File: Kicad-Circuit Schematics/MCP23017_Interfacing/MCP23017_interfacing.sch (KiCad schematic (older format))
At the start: 12 parts, among them SW1 SW_PUSH

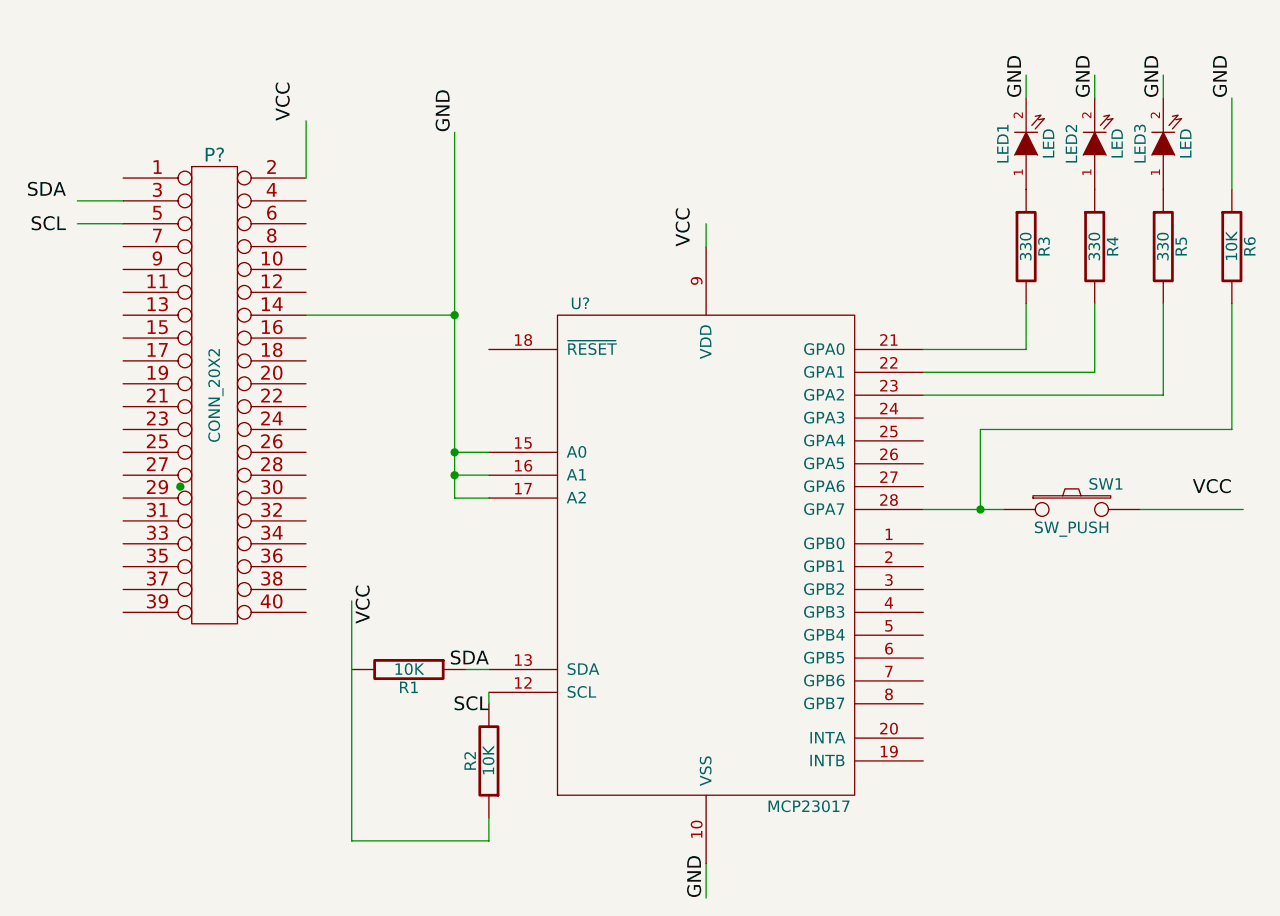
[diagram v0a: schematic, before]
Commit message: Schematics
Consists of schematics of 3 different circuits (led & push button, lcd
circuit and motor circuits)
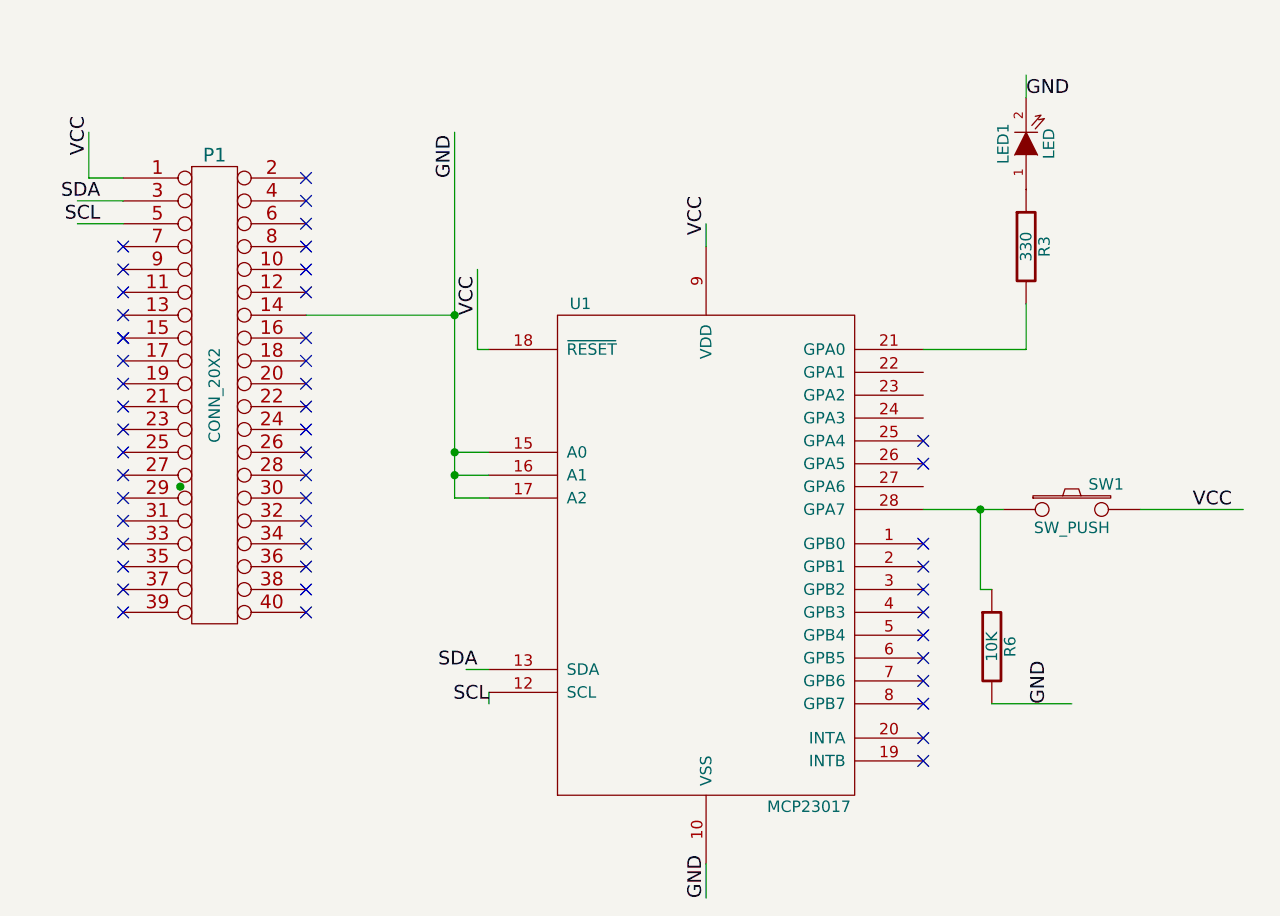
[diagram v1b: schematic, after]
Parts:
- removed LED2, LED3: LED, symbol LED
- removed R1, R2: 10K, symbol R
- removed R4, R5: 330, symbol R
- gave numbers to parts that had none: 2
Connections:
- wire segments 30 -> 23
- no-connect marks 0 -> 49
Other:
- moved on the sheet: R6
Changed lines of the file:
@@
-EESchema Schematic File Version 2  date 16-Jun-15 2:01:25 AM
+EESchema Schematic File Version 2  date 26/06/2015 16:15:03
 LIBS:power
 LIBS:device
@@
 LIBS:contrib
 LIBS:valves
-LIBS:analogSpice
-LIBS:analogXSpice
-LIBS:convergenceAidSpice
-LIBS:converterSpice
-LIBS:digitalSpice
-LIBS:digitalXSpice
-LIBS:linearSpice
-LIBS:measurementSpice
-LIBS:portSpice
-LIBS:sourcesSpice
 LIBS:MCP23017
-EELAYER 43  0
+LIBS:MCP23017_interfacing-cache
+EELAYER 25  0
 EELAYER END
 $Descr A4 11700 8267
@@
 Sheet 1 1
 Title ""
-Date "15 jun 2015"
+Date "26 jun 2015"
 Rev ""
 Comp ""
@@
 Comment4 ""
 $EndDescr
-Text Label 5250 4250 2    60   ~ 0
-SCL
-Text Label 5250 4050 2    60   ~ 0
-SDA
-Text Label 4750 3850 1    60   ~ 0
-VCC
-Wire Wire Line
-	4650 4800 5250 4800
-Wire Wire Line
-	4650 3750 4650 4800
+Text Label 6200 2150 1    60   ~ 0
+VCC
+Wire Wire Line
+	5200 2300 5200 2650
+Wire Wire Line
+	5200 2650 5250 2650
+Wire Wire Line
+	5100 1700 5100 3300
 Connection ~ 5100 3200
 Wire Wire Line
-	5250 3300 5100 3300
-Wire Wire Line
-	4450 1900 4450 1650
+	5100 3300 5250 3300
 Connection ~ 7400 3350
 Wire Wire Line
-	7400 3350 7400 3000
-Wire Wire Line
-	7400 3000 8500 3000
-Wire Wire Line
-	8500 3000 8500 2450
-Wire Wire Line
 	8100 3350 8550 3350
 Wire Wire Line
 	6200 2200 6200 2100
 Wire Wire Line
-	7900 1550 7900 1450
-Wire Wire Line
-	8200 2450 8200 2850
-Wire Wire Line
-	8200 2850 7150 2850
-Wire Wire Line
 	7600 2450 7600 2650
 Wire Wire Line
@@
 Wire Wire Line
 	6200 4900 6200 5050
-Wire Wire Line
-	5250 4800 5250 4700
 Wire Wire Line
 	5100 2500 4450 2500
@@
 	3650 2100 3450 2100
 Wire Wire Line
-	7150 2750 7900 2750
-Wire Wire Line
-	7900 2750 7900 2450
-Wire Wire Line
 	7600 1550 7600 1450
 Wire Wire Line
-	8200 1550 8200 1450
-Wire Wire Line
 	7500 3350 7150 3350
-Wire Wire Line
-	8500 1550 8500 1950
 Wire Wire Line
 	5100 3100 5250 3100
@@
 	5100 3200 5250 3200
 Connection ~ 5100 3100
-Wire Wire Line
-	5100 3300 5100 1700
 Connection ~ 5100 2500
-$Comp
-L MCP23017 U?
+Wire Wire Line
+	7400 3350 7400 3700
+Wire Wire Line
+	7400 3700 7450 3700
+Wire Wire Line
+	7450 4200 7800 4200
+Wire Wire Line
+	3650 1900 3500 1900
+Wire Wire Line
+	3500 1900 3500 1700
+Text Label 7600 1550 0    60   ~ 0
+GND
+NoConn ~ 7150 3050
+NoConn ~ 7150 3150
+NoConn ~ 4450 1900
+NoConn ~ 4450 2100
+NoConn ~ 4450 2200
+NoConn ~ 4450 2300
+NoConn ~ 4450 2400
+NoConn ~ 4450 2600
+NoConn ~ 4450 2700
+NoConn ~ 4450 2800
+NoConn ~ 4450 2900
+NoConn ~ 4450 3000
+NoConn ~ 4450 3100
+NoConn ~ 4450 3200
+NoConn ~ 4450 3300
+NoConn ~ 4450 3400
+NoConn ~ 4450 3500
+NoConn ~ 4450 3600
+NoConn ~ 4450 3700
+NoConn ~ 4450 3800
+NoConn ~ 3650 3800
+NoConn ~ 3650 3700
+NoConn ~ 3650 3600
+NoConn ~ 3650 3500
+NoConn ~ 3650 3400
+NoConn ~ 3650 3300
+NoConn ~ 3650 3200
+NoConn ~ 3650 3100
+NoConn ~ 3650 3000
+NoConn ~ 3650 2900
+NoConn ~ 3650 2800
+NoConn ~ 3650 2700
+NoConn ~ 3650 2600
+NoConn ~ 3650 2600
+NoConn ~ 3650 2500
+NoConn ~ 3650 2400
+NoConn ~ 3650 2300
+NoConn ~ 3650 2200
+NoConn ~ 4450 2000
+NoConn ~ 7150 4450
+NoConn ~ 7150 4350
+NoConn ~ 7150 4200
+NoConn ~ 7150 4100
+NoConn ~ 7150 4000
+NoConn ~ 7150 3900
+NoConn ~ 7150 3800
+NoConn ~ 7150 3700
+NoConn ~ 7150 3600
+NoConn ~ 7150 3500
+Text Label 7700 4200 1    60   ~ 0
+GND
+Text Label 5100 1900 1    60   ~ 0
+GND
+Text Label 6200 5050 1    60   ~ 0
+GND
+Text Label 5250 4200 2    60   ~ 0
+SCL
+Text Label 5200 4050 2    60   ~ 0
+SDA
+$Comp
+L MCP23017 U1
 U 1 1 557F10CB
 P 6200 3550
-F 0 "U?" H 5650 4650 50  0000 C CNN
+F 0 "U1" H 5650 4650 50  0000 C CNN
 F 1 "MCP23017" H 6650 2450 50  0000 C CNN
 F 2 "MODULE" H 5700 2450 50  0001 C CNN
@@
 	1    0    0    -1
 $EndComp
-Text Label 5100 1700 1    60   ~ 0
-GND
-Text Label 4400 1650 1    60   ~ 0
-VCC
-Text Label 8500 1550 1    60   ~ 0
-GND
+Text Label 3500 1800 1    60   ~ 0
+VCC
 $Comp
 L R R6
 U 1 1 557F310C
-P 8500 2200
-F 0 "R6" V 8580 2200 50  0000 C CNN
-F 1 "10K" V 8500 2200 50  0000 C CNN
-	1    8500 2200
-	1    0    0    -1
-$EndComp
-Text Label 8500 3300 2    60   ~ 0
+P 7450 3950
+F 0 "R6" V 7530 3950 50  0000 C CNN
+F 1 "10K" V 7450 3950 50  0000 C CNN
+	1    7450 3950
+	1    0    0    -1
+$EndComp
+Text Label 8500 3350 2    60   ~ 0
 VCC
 $Comp
@@
 	1    0    0    -1
 $EndComp
-Text Label 6150 2200 1    60   ~ 0
-VCC
-Text Label 8200 1550 1    60   ~ 0
-GND
-Text Label 7900 1550 1    60   ~ 0
-GND
-Text Label 7600 1550 1    60   ~ 0
-GND
-$Comp
-L R R5
-U 1 1 557F29FB
-P 8200 2200
-F 0 "R5" V 8280 2200 50  0000 C CNN
-F 1 "330" V 8200 2200 50  0000 C CNN
-	1    8200 2200
-	1    0    0    -1
-$EndComp
-$Comp
-L R R4
-U 1 1 557F29F5
-P 7900 2200
-F 0 "R4" V 7980 2200 50  0000 C CNN
-F 1 "330" V 7900 2200 50  0000 C CNN
-	1    7900 2200
-	1    0    0    -1
-$EndComp
+Text Label 5200 2500 1    60   ~ 0
+VCC
 $Comp
 L R R3
@@
 	1    7600 2200
 	1    0    0    -1
-$EndComp
-$Comp
-L LED LED3
-U 1 1 557F2837
-P 8200 1750
-F 0 "LED3" H 8200 1850 50  0000 C CNN
-F 1 "LED" H 8200 1650 50  0000 C CNN
-	1    8200 1750
-	0    -1   -1   0
-$EndComp
-$Comp
-L LED LED2
-U 1 1 557F2824
-P 7900 1750
-F 0 "LED2" H 7900 1850 50  0000 C CNN
-F 1 "LED" H 7900 1650 50  0000 C CNN
-	1    7900 1750
-	0    -1   -1   0
 $EndComp
 $Comp
@@
 	0    -1   -1   0
 $EndComp
-Text Label 6200 5050 1    60   ~ 0
-GND
-Text Label 3400 2150 2    60   ~ 0
+Text Label 3550 2100 2    60   ~ 0
 SCL
-Text Label 3400 2000 2    60   ~ 0
+Text Label 3550 2000 2    60   ~ 0
 SDA
 $Comp
-L R R2
-U 1 1 557F1CC8
-P 5250 4450
-F 0 "R2" V 5330 4450 50  0000 C CNN
-F 1 "10K" V 5250 4450 50  0000 C CNN
-	1    5250 4450
-	-1   0    0    1
-$EndComp
-$Comp
-L R R1
-U 1 1 557F1C73
-P 4900 4050
-F 0 "R1" V 4980 4050 50  0000 C CNN
-F 1 "10K" V 4900 4050 50  0000 C CNN
-	1    4900 4050
-	0    1    1    0
-$EndComp
-$Comp
-L CONN_20X2 P?
+L CONN_20X2 P1
 U 1 1 557F1115
 P 4050 2850
-F 0 "P?" H 4050 3900 60  0000 C CNN
+F 0 "P1" H 4050 3900 60  0000 C CNN
 F 1 "CONN_20X2" V 4050 2850 50  0000 C CNN
 	1    4050 2850

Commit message: Final designs added
Contains the pcb layout and schematics of 3 stacks
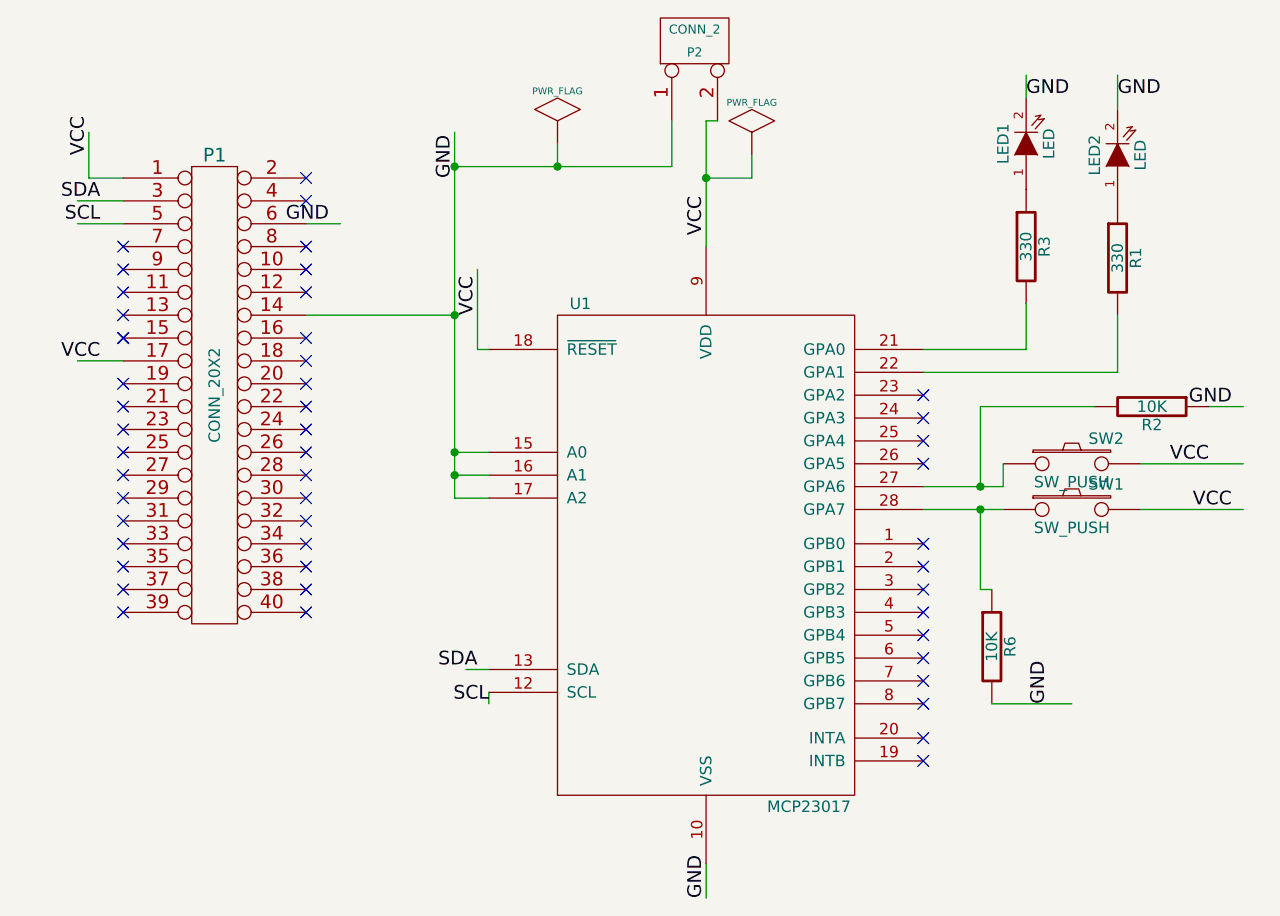
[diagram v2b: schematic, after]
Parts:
- added LED2: LED, symbol LED
- added P2: CONN_2, symbol CONN_2
- added R1: 330, symbol R
- added R2: 10K, symbol R
- added SW2: SW_PUSH, symbol SW_PUSH
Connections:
- wire segments 23 -> 40
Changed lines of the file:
@@
-EESchema Schematic File Version 2  date 26/06/2015 16:15:03
+EESchema Schematic File Version 2  date 07/07/2015 16:55:25
 LIBS:power
 LIBS:device
@@
 Sheet 1 1
 Title ""
-Date "26 jun 2015"
+Date "7 jul 2015"
 Rev ""
 Comp ""
@@
 Comment4 ""
 $EndDescr
-Text Label 6200 2150 1    60   ~ 0
+Text Label 3550 2700 2    60   ~ 0
 VCC
+Wire Wire Line
+	3650 2700 3450 2700
+Connection ~ 5550 1850
+Wire Wire Line
+	5550 1750 5550 1850
+Wire Wire Line
+	6250 1650 6200 1650
+Wire Wire Line
+	6200 1650 6200 2200
+Wire Wire Line
+	7900 2900 7400 2900
+Connection ~ 7400 3250
+Wire Wire Line
+	7400 2900 7400 3250
+Wire Wire Line
+	7500 3150 7500 3250
+Wire Wire Line
+	8000 2500 8000 2750
+Wire Wire Line
+	8000 2750 7150 2750
+Wire Wire Line
+	8000 1600 8000 1450
 Wire Wire Line
 	5200 2300 5200 2650
@@
 	8100 3350 8550 3350
 Wire Wire Line
-	6200 2200 6200 2100
-Wire Wire Line
 	7600 2450 7600 2650
 Wire Wire Line
@@
 Wire Wire Line
 	5100 2500 4450 2500
-Connection ~ 3900 3250
 Wire Wire Line
 	5250 4150 5250 4200
@@
 Wire Wire Line
 	3500 1900 3500 1700
+Wire Wire Line
+	7500 3250 7150 3250
+Wire Wire Line
+	8100 3150 8550 3150
+Wire Wire Line
+	8400 2900 8550 2900
+Wire Wire Line
+	5100 1850 6050 1850
+Connection ~ 5100 1850
+Wire Wire Line
+	6050 1850 6050 1650
+Wire Wire Line
+	6200 1900 6400 1900
+Wire Wire Line
+	6400 1900 6400 1800
+Connection ~ 6200 1900
+Wire Wire Line
+	4450 2100 4600 2100
+Text Label 4550 2100 2    60   ~ 0
+GND
+NoConn ~ 4450 2200
+$Comp
+L PWR_FLAG #FLG01
+U 1 1 559B7CE2
+P 5550 1750
+F 0 "#FLG01" H 5550 2020 30  0001 C CNN
+F 1 "PWR_FLAG" H 5550 1980 30  0000 C CNN
+	1    5550 1750
+	1    0    0    -1
+$EndComp
+$Comp
+L PWR_FLAG #FLG02
+U 1 1 559B7CA6
+P 6400 1800
+F 0 "#FLG02" H 6400 2070 30  0001 C CNN
+F 1 "PWR_FLAG" H 6400 2030 30  0000 C CNN
+	1    6400 1800
+	1    0    0    -1
+$EndComp
+$Comp
+L CONN_2 P2
+U 1 1 559B7C4D
+P 6150 1300
+F 0 "P2" V 6100 1300 40  0000 C CNN
+F 1 "CONN_2" V 6200 1300 40  0000 C CNN
+	1    6150 1300
+	0    -1   -1   0
+$EndComp
+Text Label 5250 4200 2    60   ~ 0
+SCL
+Text Label 8500 2900 2    60   ~ 0
+GND
+$Comp
+L R R2
+U 1 1 559B7ADF
+P 8150 2900
+F 0 "R2" V 8230 2900 50  0000 C CNN
+F 1 "10K" V 8150 2900 50  0000 C CNN
+	1    8150 2900
+	0    1    1    0
+$EndComp
+Text Label 8400 3150 2    60   ~ 0
+VCC
+$Comp
+L SW_PUSH SW2
+U 1 1 559B7A7E
+P 7800 3150
+F 0 "SW2" H 7950 3260 50  0000 C CNN
+F 1 "SW_PUSH" H 7800 3070 50  0000 C CNN
+	1    7800 3150
+	1    0    0    -1
+$EndComp
+Text Label 8000 1550 0    60   ~ 0
+GND
+$Comp
+L LED LED2
+U 1 1 559B79EB
+P 8000 1800
+F 0 "LED2" H 8000 1900 50  0000 C CNN
+F 1 "LED" H 8000 1700 50  0000 C CNN
+	1    8000 1800
+	0    -1   -1   0
+$EndComp
+$Comp
+L R R1
+U 1 1 559B79E6
+P 8000 2250
+F 0 "R1" V 8080 2250 50  0000 C CNN
+F 1 "330" V 8000 2250 50  0000 C CNN
+	1    8000 2250
+	1    0    0    -1
+$EndComp
+NoConn ~ 7150 2850
+NoConn ~ 7150 2950
+Text Label 6200 2150 1    60   ~ 0
+VCC
 Text Label 7600 1550 0    60   ~ 0
 GND
@@
 NoConn ~ 7150 3150
 NoConn ~ 4450 1900
-NoConn ~ 4450 2100
-NoConn ~ 4450 2200
 NoConn ~ 4450 2300
 NoConn ~ 4450 2400
@@
 NoConn ~ 3650 2900
 NoConn ~ 3650 2800
-NoConn ~ 3650 2700
 NoConn ~ 3650 2600
 NoConn ~ 3650 2600
@@
 Text Label 6200 5050 1    60   ~ 0
 GND
-Text Label 5250 4200 2    60   ~ 0
-SCL
 Text Label 5200 4050 2    60   ~ 0
 SDA
